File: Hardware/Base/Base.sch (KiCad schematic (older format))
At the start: 8 parts

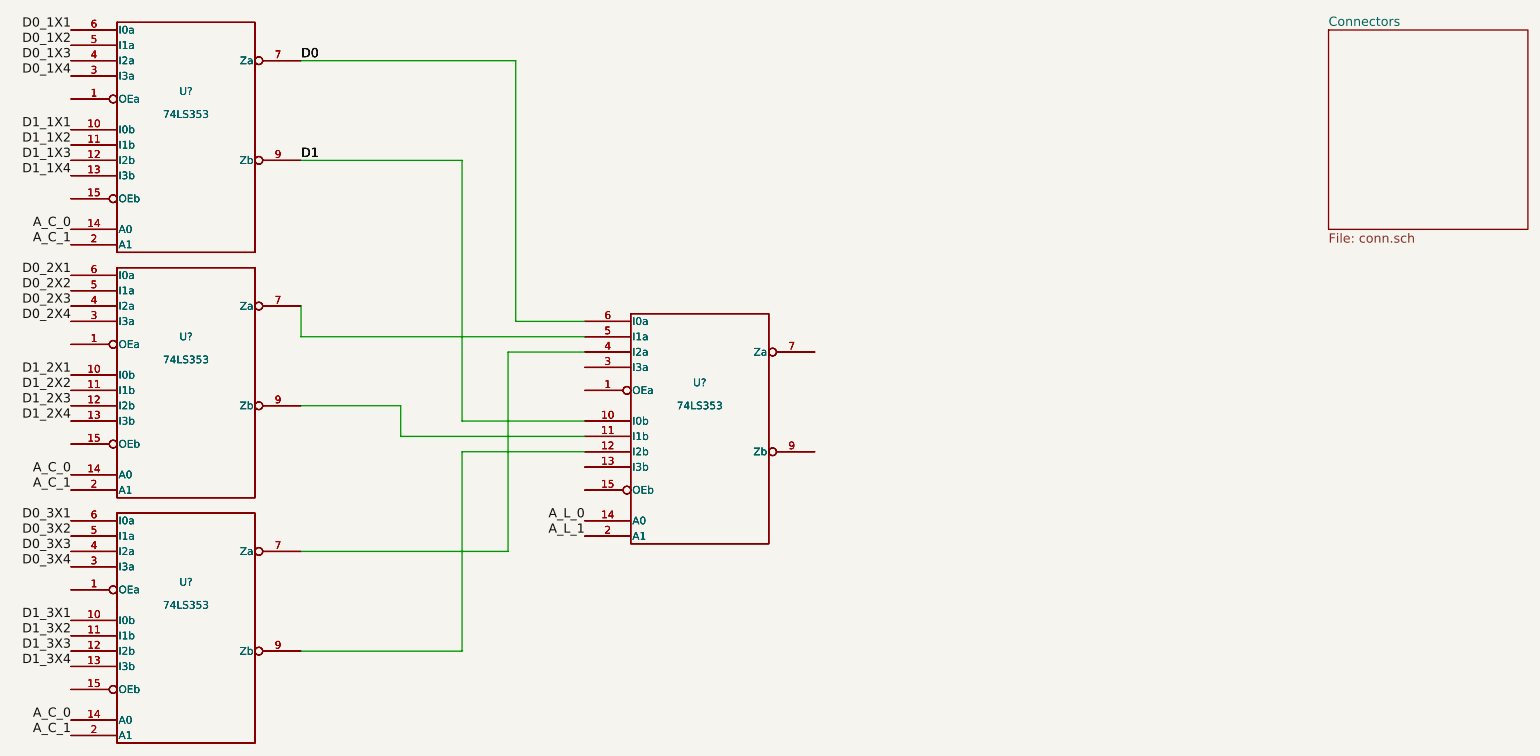
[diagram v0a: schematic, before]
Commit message: Hardware: Start the base PCB
Signed-off-by: Paul Kocialkowski <contact@paulk.fr>
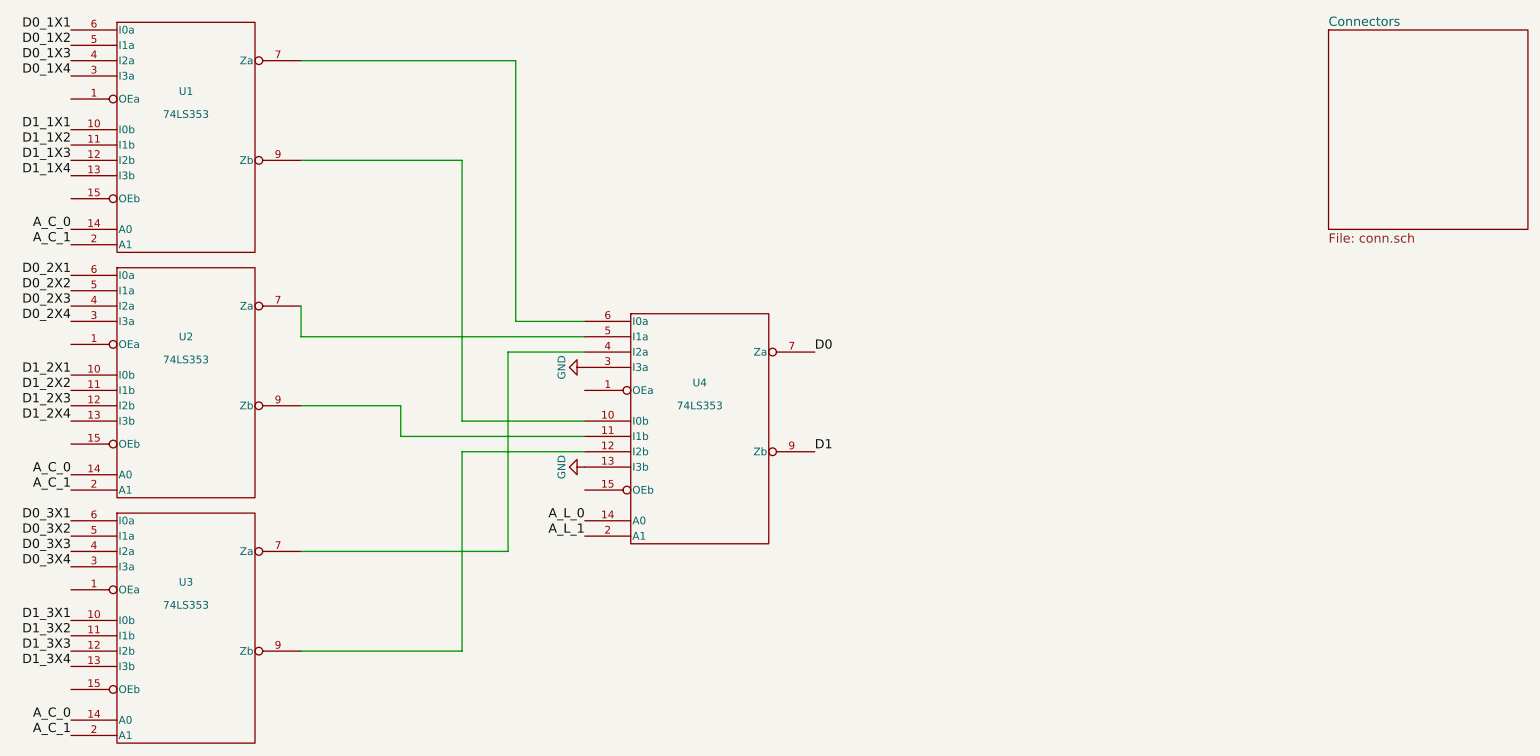
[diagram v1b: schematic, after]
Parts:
- removed U? (x4): 74LS353, symbol 74LS353
- U1, U2, U3, U4: renamed from U?; footprint (none) -> Housings_SSOP:TSSOP-16_4.4x5mm_Pitch0.65mm
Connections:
- net D0: now also U4.7 (Za); no longer U1.7 (Za), U4.6 (I0a)
- net D1: now also U4.9 (Zb); no longer U1.9 (Zb), U4.10 (I0b)
- net GND: now also U4.13 (I3b), U4.3 (I3a)
- new net: U1.7 (Za), U4.6 (I0a)
- new net: U1.9 (Zb), U4.10 (I0b)
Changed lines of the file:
@@
 Comment4 ""
 $EndDescr
-$Comp
-L 74LS353 U?
-U 1 1 58EF2C3F
-P 2050 1550
-F 0 "U?" H 2050 1850 50  0000 C CNN
-F 1 "74LS353" H 2050 1700 50  0000 C CNN
-F 2 "" H 2050 1550 50  0000 C CNN
-F 3 "" H 2050 1550 50  0000 C CNN
-	1    2050 1550
-	1    0    0    -1
-$EndComp
-$Comp
-L 74LS353 U?
-U 1 1 58EF2C6E
-P 2050 3150
-F 0 "U?" H 2050 3450 50  0000 C CNN
-F 1 "74LS353" H 2050 3300 50  0000 C CNN
-F 2 "" H 2050 3150 50  0000 C CNN
-F 3 "" H 2050 3150 50  0000 C CNN
-	1    2050 3150
-	1    0    0    -1
-$EndComp
-$Comp
-L 74LS353 U?
-U 1 1 5901881A
-P 2050 4750
-F 0 "U?" H 2050 5050 50  0000 C CNN
-F 1 "74LS353" H 2050 4900 50  0000 C CNN
-F 2 "" H 2050 4750 50  0000 C CNN
-F 3 "" H 2050 4750 50  0000 C CNN
-	1    2050 4750
-	1    0    0    -1
-$EndComp
-Text Label 2800 1050 0    60   ~ 0
-D0
-Text Label 2800 1700 0    60   ~ 0
-D1
-$Comp
-L 74LS353 U?
-U 1 1 590190D3
-P 5400 3450
-F 0 "U?" H 5400 3750 50  0000 C CNN
-F 1 "74LS353" H 5400 3600 50  0000 C CNN
-F 2 "" H 5400 3450 50  0000 C CNN
-F 3 "" H 5400 3450 50  0000 C CNN
-	1    5400 3450
-	1    0    0    -1
-$EndComp
 Wire Wire Line
 	2800 1050 4200 1050
@@
 	3850 4900 2800 4900
 $Comp
-L 74LS353 U?
+L 74LS353 U1
 U 1 1 59019BD7
 P 2050 1550
-F 0 "U?" H 2050 1850 50  0000 C CNN
+F 0 "U1" H 2050 1850 50  0000 C CNN
 F 1 "74LS353" H 2050 1700 50  0000 C CNN
-F 2 "" H 2050 1550 50  0000 C CNN
+F 2 "Housings_SSOP:TSSOP-16_4.4x5mm_Pitch0.65mm" H 2050 1550 50  0001 C CNN
 F 3 "" H 2050 1550 50  0000 C CNN
 	1    2050 1550
@@
 $EndComp
 $Comp
-L 74LS353 U?
+L 74LS353 U2
 U 1 1 59019BD8
 P 2050 3150
-F 0 "U?" H 2050 3450 50  0000 C CNN
+F 0 "U2" H 2050 3450 50  0000 C CNN
 F 1 "74LS353" H 2050 3300 50  0000 C CNN
-F 2 "" H 2050 3150 50  0000 C CNN
+F 2 "Housings_SSOP:TSSOP-16_4.4x5mm_Pitch0.65mm" H 2050 3150 50  0001 C CNN
 F 3 "" H 2050 3150 50  0000 C CNN
 	1    2050 3150
@@
 $EndComp
 $Comp
-L 74LS353 U?
+L 74LS353 U3
 U 1 1 59019BD9
 P 2050 4750
-F 0 "U?" H 2050 5050 50  0000 C CNN
+F 0 "U3" H 2050 5050 50  0000 C CNN
 F 1 "74LS353" H 2050 4900 50  0000 C CNN
-F 2 "" H 2050 4750 50  0000 C CNN
+F 2 "Housings_SSOP:TSSOP-16_4.4x5mm_Pitch0.65mm" H 2050 4750 50  0001 C CNN
 F 3 "" H 2050 4750 50  0000 C CNN
 	1    2050 4750
 	1    0    0    -1
 $EndComp
-Text Label 2800 1050 0    60   ~ 0
-D0
-Text Label 2800 1700 0    60   ~ 0
-D1
 $Comp
-L 74LS353 U?
+L 74LS353 U4
 U 1 1 59019BDB
 P 5400 3450
-F 0 "U?" H 5400 3750 50  0000 C CNN
+F 0 "U4" H 5400 3750 50  0000 C CNN
 F 1 "74LS353" H 5400 3600 50  0000 C CNN
-F 2 "" H 5400 3450 50  0000 C CNN
+F 2 "Housings_SSOP:TSSOP-16_4.4x5mm_Pitch0.65mm" H 5400 3450 50  0001 C CNN
 F 3 "" H 5400 3450 50  0000 C CNN
 	1    5400 3450
@@
 F1 "conn.sch" 60
 $EndSheet
-Text Label 1300 1500 2    60   ~ 0
-D1_1X1
 Text Label 1300 950  2    60   ~ 0
 D0_1X2
@@
 Text Label 1300 2250 2    60   ~ 0
 A_C_1
+Text Label 1300 1500 2    60   ~ 0
+D1_1X1
+Text Label 6150 2950 0    60   ~ 0
+D0
+Text Label 6150 3600 0    60   ~ 0
+D1
+$Comp
+L GND #PWR01
+U 1 1 590320A9
+P 4650 3050
+F 0 "#PWR01" H 4650 2800 50  0001 C CNN
+F 1 "GND" H 4650 2900 50  0000 C CNN
+F 2 "" H 4650 3050 50  0000 C CNN
+F 3 "" H 4650 3050 50  0000 C CNN
+	1    4650 3050
+	0    1    1    0
+$EndComp
+$Comp
+L GND #PWR02
+U 1 1 590320C5
+P 4650 3700
+F 0 "#PWR02" H 4650 3450 50  0001 C CNN
+F 1 "GND" H 4650 3550 50  0000 C CNN
+F 2 "" H 4650 3700 50  0000 C CNN
+F 3 "" H 4650 3700 50  0000 C CNN
+	1    4650 3700
+	0    1    1    0
+$EndComp
 $EndSCHEMATC
